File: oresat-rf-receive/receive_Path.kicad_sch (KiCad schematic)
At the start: 32 parts, among them J11 142-0711-201, J12 0022232021, J13 0022232021, J15 0022232041, J8 142-0711-201, U18 PAT1220-C-3DB, U23 PAT1220-C-3DB, U24 TQP3M9037, U25 PD2328J5050S2HF, U26 TQP3M9037, U27 LTC5505-1ES5, U28 SN74LVC1G32QDBVRQ1

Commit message: replaced symbol for connector with 3-pin symbol
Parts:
- removed J11, J8: 142-0711-201, oresat-connectors:SMA 142-0711-201, symbol Connector:Conn_Coaxial
- added J1, J6: Conn_Coaxial_142-0711-201, oresat-connectors:SMA 142-0711-201, symbol oresat-connectors:Conn_Coaxial_142-0711-201
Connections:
- net GND: now also J1.1 (In), J1.2 (Ext), J6.1 (In), J6.2 (Ext)
- net RF_IN: now also J6.3
- net RF_OUT: now also J1.3
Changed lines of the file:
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@@
 	)
 	(symbol
+		(lib_id "oresat-connectors:Conn_Coaxial_142-0711-201")
+		(at 16.51 107.95 0)
+		(mirror y)
+		(unit 1)
+		(exclude_from_sim no)
+		(in_bom yes)
+		(on_board yes)
+		(dnp no)
+		(fields_autoplaced yes)
+		(property "Reference" "J6"
+			(at 16.8274 101.6 0)
+			(effects
+				(font
+					(size 1.27 1.27)
+				)
+			)
+		)
+		(property "Value" "Conn_Coaxial_142-0711-201"
+			(at 16.8274 104.14 0)
+			(effects
+				(font
+					(size 1.27 1.27)
+				)
+			)
+		)
+		(property "Footprint" "oresat-connectors:SMA 142-0711-201"
+			(at 16.51 107.95 0)
+			(effects
+				(font
+					(size 1.27 1.27)
+				)
+				(hide yes)
+			)
+		)
+		(property "Datasheet" "~"
+			(at 16.51 107.95 0)
+			(effects
+				(font
+					(size 1.27 1.27)
+				)
+				(hide yes)
+			)
+		)
+		(property "Description" "coaxial connector (BNC, SMA, SMB, SMC, Cinch/RCA, LEMO, ...)"
+			(at 18.796 100.584 0)
+			(effects
+				(font
+					(size 1.27 1.27)
+				)
+				(hide yes)
+			)
+		)
+		(pin "3"
+		)
+		(pin "1"
+		)
+		(pin "2"
+		)
+		(instances
+			(project ""
+				(path "/7b213b9d-ec60-40bb-9d89-aeb6916c3ceb"
+					(reference "J6")
+					(unit 1)
+				)
+			)
+		)
+	)
+	(symbol
 		(lib_id "Device:C_Small")
 		(at 129.54 107.95 90)
@@
 	)
 	(symbol
+		(lib_id "oresat-connectors:Conn_Coaxial_142-0711-201")
+		(at 367.03 105.41 0)
+		(unit 1)
+		(exclude_from_sim no)
+		(in_bom yes)
+		(on_board yes)
+		(dnp no)
+		(property "Reference" "J1"
+			(at 366.7126 99.06 0)
+			(effects
+				(font
+					(size 1.27 1.27)
+				)
+			)
+		)
+		(property "Value" "Conn_Coaxial_142-0711-201"
+			(at 366.7126 101.6 0)
+			(effects
+				(font
+					(size 1.27 1.27)
+				)
+			)
+		)
+		(property "Footprint" "oresat-connectors:SMA 142-0711-201"
+			(at 367.03 105.41 0)
+			(effects
+				(font
+					(size 1.27 1.27)
+				)
+				(hide yes)
+			)
+		)
+		(property "Datasheet" "~"
+			(at 367.03 105.41 0)
+			(effects
+				(font
+					(size 1.27 1.27)
+				)
+				(hide yes)
+			)
+		)
+		(property "Description" "coaxial connector (BNC, SMA, SMB, SMC, Cinch/RCA, LEMO, ...)"
+			(at 364.744 98.044 0)
+			(effects
+				(font
+					(size 1.27 1.27)
+				)
+				(hide yes)
+			)
+		)
+		(pin "3"
+		)
+		(pin "1"
+		)
+		(pin "2"
+		)
+		(instances
+			(project "receive_Path"
+				(path "/7b213b9d-ec60-40bb-9d89-aeb6916c3ceb"
+					(reference "J1")
+					(unit 1)
+				)
+			)
+		)
+	)
+	(symbol
 		(lib_id "power:GND")
 		(at 212.09 120.65 0)
@@
 					(unit 1)
 				)
-			)
-		)
-	)
-	(symbol
-		(lib_id "Connector:Conn_Coaxial")
-		(at 16.51 107.95 0)
-		(mirror y)
-		(unit 1)
-		(exclude_from_sim no)
-		(in_bom yes)
-		(on_board yes)
-		(dnp no)
-		(property "Reference" "J11"
-			(at 18.288 103.378 0)
-			(effects
-				(font
-					(size 1.27 1.27)
-				)
-				(justify left)
-			)
-		)
-		(property "Value" "142-0711-201"
-			(at 30.226 118.618 0)
-			(effects
-				(font
-					(size 1.27 1.27)
-				)
-				(justify left)
-			)
-		)
-		(property "Footprint" "oresat-connectors:SMA 142-0711-201"
-			(at 16.51 107.95 0)
-			(effects
-				(font
-					(size 1.27 1.27)
-				)
-				(hide yes)
-			)
-		)
-		(property "Datasheet" "https://www.belfuse.com/resources/productinformations/cinchconnectivitysolutions/johnson/pi-ccs-john-142-0711-201.pdf"
-			(at 16.51 107.95 0)
-			(effects
-				(font
-					(size 1.27 1.27)
-				)
-				(hide yes)
-			)
-		)
-		(property "Description" "CONN SMA JACK STR 50 OHM SMD"
-			(at 16.51 107.95 0)
-			(effects
-				(font
-					(size 1.27 1.27)
-				)
-				(hide yes)
-			)
-		)
-		(property "MPN" "142-0711-201"
-			(at 16.51 107.95 0)
-			(effects
-				(font
-					(size 1.27 1.27)
-				)
-				(hide yes)
-			)
-		)
-		(property "MFR" "Cinch Connectivity Solutions Johnson"
-			(at 16.51 107.95 0)
-			(effects
-				(font
-					(size 1.27 1.27)
-				)
-				(hide yes)
-			)
-		)
-		(property "DPN" "J819-ND"
-			(at 16.51 107.95 0)
-			(effects
-				(font
-					(size 1.27 1.27)
-				)
-				(hide yes)
-			)
-		)
-		(property "Distributor" "Digi-Key"
-			(at 16.51 107.95 0)
-			(effects
-				(font
-					(size 1.27 1.27)
-				)
-				(hide yes)
-			)
-		)
-		(pin "2"
-		)
-		(pin "1"
-		)
-		(instances
-			(project "oresat-live-card"
-				(path "/748bdd2d-da0a-4240-ba60-0bf881d2ec56/59766a54-e9a6-4442-8b97-63ec20aef604"
-					(reference "J11")
-					(unit 1)
-				)
-			)
-			(project ""
-				(path "/7b213b9d-ec60-40bb-9d89-aeb6916c3ceb"
-					(reference "J1")
-					(unit 1)
-				)
-			)
-		)
-	)
-	(symbol
-		(lib_id "Connector:Conn_Coaxial")
-		(at 367.03 105.41 0)
-		(unit 1)
-		(exclude_from_sim no)
-		(in_bom yes)
-		(on_board yes)
-		(dnp no)
-		(fields_autoplaced yes)
-		(property "Reference" "J8"
-			(at 370.84 104.4331 0)
-			(effects
-				(font
-					(size 1.27 1.27)
-				)
-				(justify left)
-			)
-		)
-		(property "Value" "142-0711-201"
-			(at 370.84 106.9731 0)
-			(effects
-				(font
-					(size 1.27 1.27)
-				)
-				(justify left)
-			)
-		)
-		(property "Footprint" "oresat-connectors:SMA 142-0711-201"
-			(at 367.03 105.41 0)
-			(effects
-				(font
-					(size 1.27 1.27)
-				)
-				(hide yes)
-			)
-		)
-		(property "Datasheet" "https://www.belfuse.com/resources/productinformations/cinchconnectivitysolutions/johnson/pi-ccs-john-142-0711-201.pdf"
-			(at 367.03 105.41 0)
-			(effects
-				(font
-					(size 1.27 1.27)
-				)
-				(hide yes)
-			)
-		)
-		(property "Description" "CONN SMA JACK STR 50 OHM SMD"
-			(at 367.03 105.41 0)
-			(effects
-				(font
-					(size 1.27 1.27)
-				)
-				(hide yes)
-			)
-		)
-		(property "MPN" "142-0711-201"
-			(at 367.03 105.41 0)
-			(effects
-				(font
-					(size 1.27 1.27)
-				)
-				(hide yes)
-			)
-		)
-		(property "MFR" "Cinch Connectivity Solutions Johnson"
-			(at 367.03 105.41 0)
-			(effects
-				(font
-					(size 1.27 1.27)
-				)
-				(hide yes)
-			)
-		)
-		(property "DPN" "J819-ND"
-			(at 367.03 105.41 0)
-			(effects
-				(font
-					(size 1.27 1.27)
-				)
-				(hide yes)
-			)
-		)
-		(property "Distributor" "Digi-Key"
-			(at 367.03 105.41 0)
-			(effects
-				(font
-					(size 1.27 1.27)
-				)
-				(hide yes)
-			)
-		)
-		(pin "2"
-		)
-		(pin "1"
-		)
-		(instances
-			(project ""
-				(path "/748bdd2d-da0a-4240-ba60-0bf881d2ec56/59766a54-e9a6-4442-8b97-63ec20aef604"
-					(reference "J8")
-					(unit 1)
-				)
-			)
-			(project ""
-				(path "/7b213b9d-ec60-40bb-9d89-aeb6916c3ceb"
-					(reference "J4")
-					(unit 1)
-				)

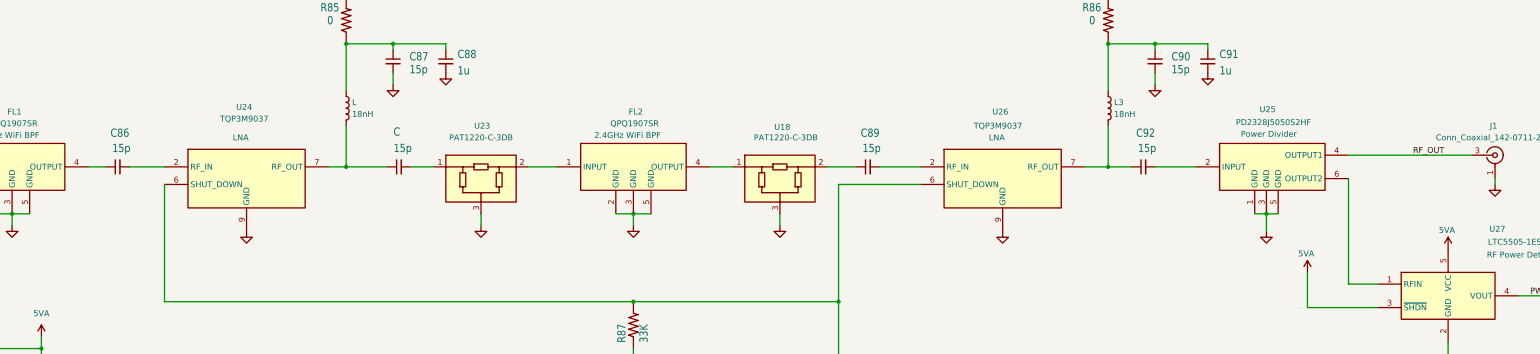
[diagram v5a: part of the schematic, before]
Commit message: update traces and net class
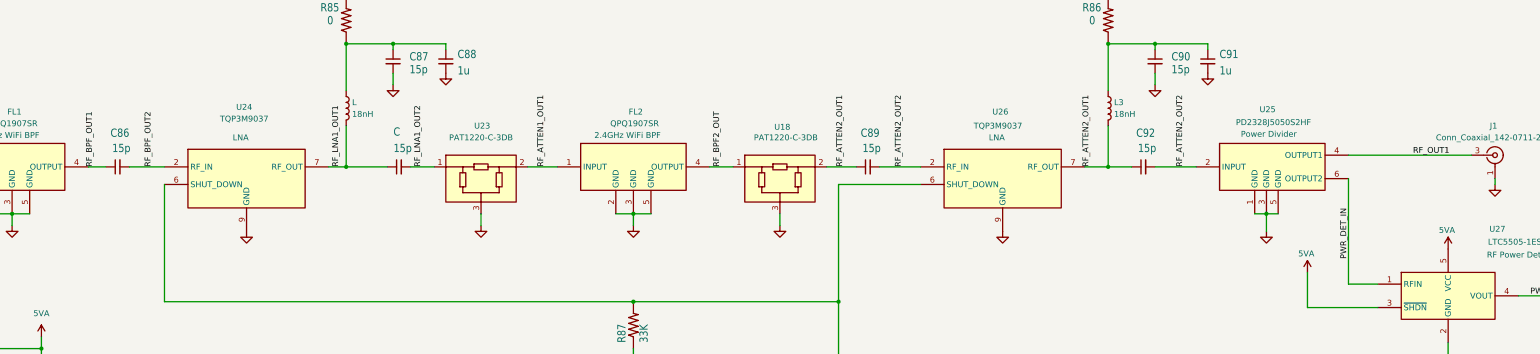
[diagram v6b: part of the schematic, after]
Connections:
- net RF_BPF2_OUT: now reaches FL2.4 (OUTPUT), U18.1
- net RF_ATTEN2_OUT1: now reaches C89.1, U18.2
- net RF_ATTEN2_OUT1: now also C92.1, L3.2, U26.7 (RF_OUT)
- net RF_LNA1_OUT2: now reaches C.2, U23.1
- net RF_ATTEN1_OUT1: now reaches FL2.1 (INPUT), U23.2
- net RF_BPF_OUT1: now reaches C86.1, FL1.4 (OUTPUT)
- net RF_BPF_OUT2: now reaches C86.2, U24.2 (RF_IN)
- net RF_ATTEN2_OUT2: now reaches C89.2, U26.2 (RF_IN)
- net RF_ATTEN2_OUT2: now also C92.2, U25.2 (INPUT)
- net PWR_DET_IN: now reaches U25.6 (OUTPUT2), U27.1 (RFIN)
- net RF_LNA1_OUT1: now reaches C.1, L.2, U24.7 (RF_OUT)
- net RF_OUT renamed RF_OUT1

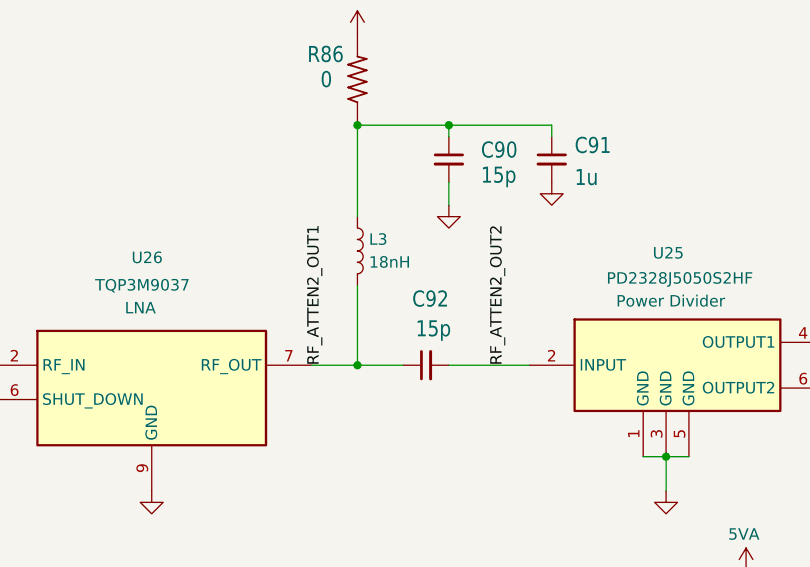
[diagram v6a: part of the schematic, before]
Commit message: Updated board layout, traces widths, and silkscreen
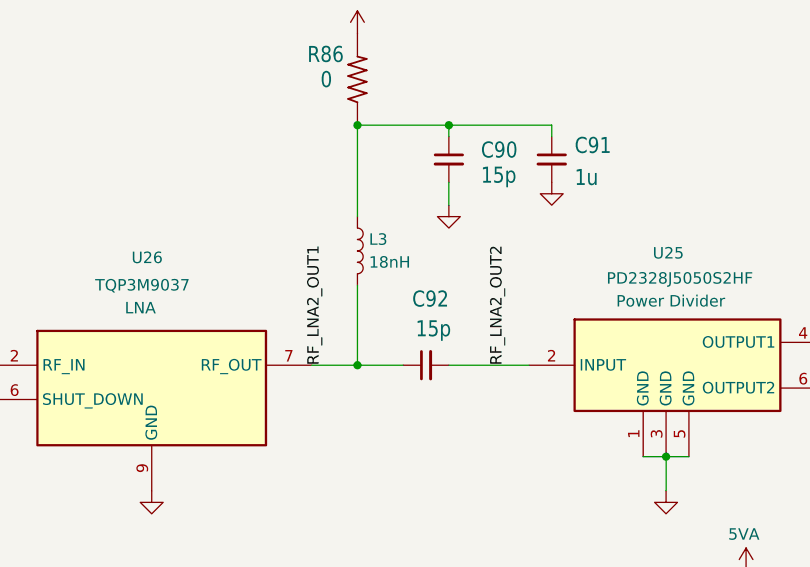
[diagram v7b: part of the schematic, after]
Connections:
- net RF_ATTEN2_OUT1: no longer C92.1, L3.2, U26.7 (RF_OUT)
- net RF_ATTEN2_OUT2: no longer C92.2, U25.2 (INPUT)
- new net RF_LNA2_OUT1: C92.1, L3.2, U26.7 (RF_OUT)
- new net RF_LNA2_OUT2: C92.2, U25.2 (INPUT)
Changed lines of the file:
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@@
 		)
 	)
-	(label "RF_ATTEN2_OUT2"
+	(label "RF_LNA2_OUT2"
 		(at 299.72 107.95 90)
 		(fields_autoplaced yes)
@@
 		)
 	)
-	(label "RF_ATTEN2_OUT1"
+	(label "RF_LNA2_OUT1"
 		(at 279.4 107.95 90)
 		(fields_autoplaced yes)

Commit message: changed reference designators for rf inputs, added ground vias, adjusted text size for designators
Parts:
- renumbered J6 to J1, J1 to J2
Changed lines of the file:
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@@
 		(dnp no)
 		(fields_autoplaced yes)
-		(property "Reference" "J6"
+		(property "Reference" "J1"
 			(at 16.8274 101.6 0)
 			(effects
@@
 			(project "receive_Path"
 				(path "/7b213b9d-ec60-40bb-9d89-aeb6916c3ceb"
-					(reference "J6")
+					(reference "J1")
 					(unit 1)
 				)
@@
 		(on_board yes)
 		(dnp no)
-		(property "Reference" "J1"
+		(property "Reference" "J2"
 			(at 366.7126 99.06 0)
 			(effects
@@
 			(project "receive_Path"
 				(path "/7b213b9d-ec60-40bb-9d89-aeb6916c3ceb"
-					(reference "J1")
+					(reference "J2")
 					(unit 1)
 				)
@@
 			(project "receive_Path"
 				(path "/7b213b9d-ec60-40bb-9d89-aeb6916c3ceb"
-					(reference "J2")
+					(reference "J4")
 					(unit 1)
 				)
